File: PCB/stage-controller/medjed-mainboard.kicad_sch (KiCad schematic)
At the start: 28 parts, among them IC1 TMC429-LI, J1 Barrel_Jack, U1 RP2040

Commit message: Add initial version stage PCB
Will probably need major revisions as efforts towards TMC4361A will require significant changes.
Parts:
- removed U1: RP2040, Package_DFN_QFN:QFN-56-1EP_7x7mm_P0.4mm_EP3.2x3.2mm, symbol MCU_RaspberryPi:RP2040
- added C10, C11, C16, C7, C8, C9: 100nF, Capacitor_SMD:C_0603_1608Metric, symbol Device:C
- added C12, C17, C18, C19: 10uF, Capacitor_SMD:C_0805_2012Metric, symbol Device:C
- added C13: 22uF, Capacitor_SMD:C_0805_2012Metric, symbol Device:C
- added C14, C15, C20, C21: 1uF, Capacitor_SMD:C_0402_1005Metric, symbol Device:C
- added D1: SMAJ28CA, medjed-mainboard:SMAJ28CA, symbol Diode:5KPxxCA
- added D2, D3, D4, D5, D6, D7, D8: Red, LED_SMD:LED_0805_2012Metric, symbol Device:LED
- added F1: SMDC185F/33-2, medjed-mainboard:SMDC185F_33-2, symbol Device:Polyfuse
- added FB1: FerriteBead, medjed-mainboard:BLM41P600S, symbol Device:FerriteBead
- added J2: Conn_01x05, Connector_PinSocket_2.54mm:PinSocket_1x05_P2.54mm_Vertical, symbol Connector_Generic:Conn_01x05
- added JP1, JP5: SolderJumper_2_Open, Jumper:SolderJumper-2_P1.3mm_Open_RoundedPad1.0x1.5mm, symbol Jumper:SolderJumper_2_Open
- added JP2, JP3, JP4, JP6: SolderJumper_2_Bridged, Jumper:SolderJumper-2_P1.3mm_Bridged_RoundedPad1.0x1.5mm, symbol Jumper:SolderJumper_2_Bridged
- added R10, R11, R12, R14, R16, R17, R18: 5k1, Resistor_SMD:R_0603_1608Metric, symbol Device:R
- added R13, R15: 10k, Resistor_SMD:R_0603_1608Metric, symbol Device:R
- added SW1: SW_Push_SPDT, medjed-mainboard:switch_SS3NP-MS-V-TR, symbol Switch:SW_Push_SPDT
- added TP1, TP2, TP3, TP4, TP5, TP6: TestPoint_Small, TestPoint:TestPoint_Pad_D1.0mm, symbol Connector:TestPoint_Small
- added TP10, TP7, TP8, TP9: TestPoint, TestPoint:TestPoint_Pad_D1.0mm, symbol Connector:TestPoint
- added U1: P78E-1000, medjed-mainboard:P78E-1000, symbol medjed-mainboard:P78E05-1000
- added U11: teensy 4.1, medjed-mainboard:teensy_4.1, symbol medjed-mainboard:teensy 4.1
- added U12: MIC5317-3.3, Package_TO_SOT_SMD:SOT-23-5, symbol medjed-mainboard:MIC5317-3.3
- added U13: MIC5317-1.5, Package_TO_SOT_SMD:SOT-23-5, symbol medjed-mainboard:MIC5317-3.3
- J1: Voltage (none) -> 24V
- renumbered U7 to U5, U5 to U7
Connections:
- net +5V: now also C10.2, C11.2, C13.1, C14.1, C17.1, C18.1, C19.1, C20.1, C9.2, D3.2 (A), JP6.2 (B), TP7.1, U1.3 (Vout), U12.1 (Vin), U12.3 (EN), U13.1 (Vin), U13.3 (EN)
- net EN motors: now also SW1.2 (B)
- net GND: now also IC1.33 (DIE_PAD), ICe1.1 (GND@1), ICe1.12 (GND@3), ICe1.25 (GND@4), ICe1.38 (GND@5), ICe1.47 (TCK), ICe1.48 (TDI), ICe1.51 (GND@6), ICe1.67 (GND@7), ICe1.75 (GND@8), ICe1.88 (GND@9), ICe1.9 (GND@2), J1.2, U5.4 (GND), C10.1, C11.1, C12.2, C13.2, C14.2, C15.2, C16.2, C17.2, C18.2, C19.2, C20.2, C21.2, C7.2, C8.2, C9.1, D1.1 (A1), JP1.1 (A), JP5.1 (A), R10.2, R11.2, R12.2, R14.2, R16.2, R17.2, R18.2, U1.2 (GND), U11.GND1 (GND), U11.GND2 (GND), U11.GND3 (GND), U11.GND4 (GND), U11.GND5 (GND), U12.2 (GND), U13.2 (GND); no longer IC1.EXP (DIE_PAD)
- net X_Z-: now reaches R2.1, U8.1 (1B)
- net X_Z-: now also U5.11 (Z-); no longer U7.11 (Z-)
- net X_A+: now reaches R3.2, U8.10 (3A)
- net X_A+: now also U5.5 (A+); no longer U7.5 (A+)
- net ENC_A_X: now reaches U8.11 (3Y)
- net ENC_A_X: now also ICe1.10 (ENC3_A); no longer ICe1.3 (ENC1_A)
- net X_Z+: now reaches R2.2, U8.2 (1A)
- net X_Z+: now also U5.10 (Z+); no longer U7.10 (Z+)
- net ENC_N_X: now reaches U8.3 (1Y)
- net ENC_N_X: now also ICe1.13 (ENC3_N); no longer ICe1.5 (ENC1_N)
- net ENC_B_X: now reaches U8.5 (2Y)
- net ENC_B_X: now also ICe1.11 (ENC3_B); no longer ICe1.4 (ENC1_B)
- net X_B+: now reaches R1.2, U8.6 (2A)
- net X_B+: now also U5.7 (B+); no longer U7.7 (B+)
- net X_B-: now reaches R1.1, U8.7 (2B)
- net X_B-: now also U5.8 (B-); no longer U7.8 (B-)
- net X_A-: now reaches R3.1, U8.9 (3B)
- net X_A-: now also U5.6 (A-); no longer U7.6 (A-)
- net Z_Z+: now reaches R7.2, U10.2 (1A)
- net Z_Z+: now also U7.10 (Z+); no longer U5.10 (Z+)
- net Z_Z-: now reaches R7.1, U10.1 (1B)
- net Z_Z-: now also U7.11 (Z-); no longer U5.11 (Z-)
- net Z_A+: now reaches R9.2, U10.10 (3A)
- net Z_A+: now also U7.5 (A+); no longer U5.5 (A+)
- net Z_A-: now reaches R9.1, U10.9 (3B)
- net Z_A-: now also U7.6 (A-); no longer U5.6 (A-)
- net Z_B+: now reaches R8.2, U10.6 (2A)
- net Z_B+: now also U7.7 (B+); no longer U5.7 (B+)
- net Z_B-: now reaches R8.1, U10.7 (2B)
- net Z_B-: now also U7.8 (B-); no longer U5.8 (B-)
- net DIR-Z: now reaches IC1.17 (SCK_S_D1), U3.5 (DIR)
- net DIR-Z: now also TP5.1
- net STEP-Z: now reaches IC1.15 (SDO_S_S1), U3.6 (STEP)
- net STEP-Z: now also TP6.1
- net +24V: now reaches C5.2, C6.1, U3.7 (+24V)
- net +24V: now also C1.2, C2.1, C3.2, C4.1, U2.7 (+24V), U4.7 (+24V), C12.1, C8.1, D2.2 (A), FB1.2, TP8.1, U1.1 (Vin)
- net +24Vsrc: now reaches J1.1
- net +24Vsrc: now also F1.1
- net MOSI: now reaches IC1.10 (SDI_C), ICe1.99 (SDI)
- net MOSI: now also J2.4 (Pin_4), U11.26 (A12)
- net SDO-429: now reaches IC1.12 (SDOZ_C), ICe1.96 (SDO429)
- net SDO-429: now also JP2.1 (A)
- net INT_429: now reaches IC1.14 (~{INT_SDO_C})
- net INT_429: now also U11.10 (CS1)
- net STEP-Y: now reaches IC1.18 (~{SCS_S_S2}), U2.6 (STEP)
- net STEP-Y: now also TP3.1
- net STEP-X: now reaches IC1.19 (~{SCS2_S3}), U4.6 (STEP)
- net STEP-X: now also TP1.1
- net DIR-X: now reaches IC1.20 (~{SCS3_D3}), U4.5 (DIR)
- net DIR-X: now also TP2.1
- net +3.3V: now reaches IC1.21 (V5@2)
- net +3.3V: now also IC1.22 (V33), IC1.3 (V5@1), ICe1.18 (VCCI@1), ICe1.24 (VCC@1), ICe1.39 (VCCI@2), ICe1.50 (VCC@2), ICe1.52 (VCC@3), ICe1.56 (VCC@4), ICe1.66 (VCCI@3), ICe1.74 (VCC@5), ICe1.87 (VCCI@4), C15.1, C16.1, D4.2 (A), JP3.2 (B), JP4.1 (A), R13.1, TP9.1, U12.5 (Vout)
- net DIR-Y: now reaches IC1.27 (SDI_S_D2), U2.5 (DIR)
- net DIR-Y: now also TP4.1
- net POSCMP: now reaches IC1.30 (POSCMP)
- net POSCMP: now also D5.2 (A)
- net TeensyCLK: now reaches IC1.5 (CLK)
- net TeensyCLK: now also ICe1.64 (CLK), U11.40 (A16)
- net CS429: now reaches IC1.7 (~{SCS_C}), ICe1.95 (~{SCS429})
- net CS429: now also J2.1 (Pin_1), U11.25 (A11)
- net SCK: now reaches IC1.8 (SCK_C), ICe1.98 (SCK)
- net SCK: now also J2.3 (Pin_3), U11.27 (A13)
- net ENC_A_Z: now reaches U10.11 (3Y)
- net ENC_A_Z: now also ICe1.3 (ENC1_A); no longer ICe1.10 (ENC3_A)
- net MISO: now reaches ICe1.100 (SDO)
- net MISO: now also J2.5 (Pin_5), JP2.2 (B), U11.39 (A15)
- net ENC_B_Z: now reaches U10.5 (2Y)
- net ENC_B_Z: now also ICe1.4 (ENC1_B); no longer ICe1.11 (ENC3_B)
- net ENC_N_Z: now reaches U10.3 (1Y)
- net ENC_N_Z: now also ICe1.5 (ENC1_N); no longer ICe1.13 (ENC3_N)
- net +1V5: now reaches ICe1.14 (VCORE@1)
- net +1V5: now also ICe1.17 (VCORE@2), ICe1.37 (VCORE@3), ICe1.68 (VCORE@4), ICe1.89 (VCORE@5), C21.1, TP10.1, U13.5 (Vout)
- net at ICe1.49 (TMS): now also ICe1.55 (TRST), R13.2
- net ENC_A_Y: now reaches ICe1.6 (ENC2_A), U9.11 (3Y)
- net ENC_B_Y: now reaches ICe1.7 (ENC2_B), U9.5 (2Y)
- net ENC_N_Y: now reaches ICe1.8 (ENC2_N), U9.3 (1Y)
- net at ICe1.86 (ENC_INV): now also JP1.2 (B)
- net at ICe1.92 (EXT_RES): now also JP3.1 (A)
- net INT_424: now reaches ICe1.94 (~{INT})
- net INT_424: now also U11.16 (A2)
- net CS424: now reaches ICe1.97 (~{SCS})
- net CS424: now also J2.2 (Pin_2), U11.38 (A14)
- net Y_Z-: now reaches R4.1, U6.11 (Z-), U9.1 (1B)
- net Y_Z+: now reaches R4.2, U6.10 (Z+), U9.2 (1A)
- net Y_A+: now reaches R6.2, U6.5 (A+), U9.10 (3A)
- net Y_B+: now reaches R5.2, U6.7 (B+), U9.6 (2A)
- net Y_B-: now reaches R5.1, U6.8 (B-), U9.7 (2B)
- net Y_A-: now reaches R6.1, U6.6 (A-), U9.9 (3B)
- new net: D3.1 (K), R10.1
- new net: R15.1, SW1.1 (A)
- new net: D7.1 (K), R17.1
- new net: D4.1 (K), R12.1
- new net: D2.1 (K), R11.1
- new net: D8.1 (K), R18.1
- new net: D5.1 (K), R14.1
- new net: U11.3.3V_1 (3.3V), U11.3.3V_2 (3.3V), U11.3.3V_3 (3.3V)
- new net: U11.USB_GND1 (USB_GND), U11.USB_GND2 (USB_GND)
- new net: JP6.1 (A), U11.VIN
- new net: D6.1 (K), R16.1
- new net +24Vfused: C7.1, D1.2 (A2), F1.2, FB1.1
- new net HomeX: D6.2 (A), U11.36 (CS2)
- new net HomeY: D7.2 (A), U11.35 (TX8)
- new net HomeZ: D8.2 (A), U11.34 (RX8)
- new net STEPPER_EN: SW1.3 (C), U11.33 (MCLK2)
- new net STEP_EN_MANUAL: JP4.2 (B), JP5.2 (B), R15.2
- no-connect marks 6 -> 30
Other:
- note added: "0.0.1"
- note added: "27-04-2023"
- note added: "Figure out GBAR stuff"
- note added: "Medjed Stage Controller Board"
- note added: "PWM clock signal 18.75MHz?"
- note added: "Remember to cut solder jumper on Teensy if powering from 5V"
- note added: "Run in 3.3V supply mode (CMOS)"
- note added: "TMC2209 is off with ENN input high Unknown if Snapmaker EN is inverted"
- note added: "TODO: remove bridged jumper"
- note added: "To be used with Teensy 4.1 board"
- note added: "should not be needed"
- note removed: "handle these two"
- moved on the sheet: C1, C2, C3, C4, C5, C6, ICe1, J1, R1, R2, R3, R4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

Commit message: New TMC4361 design
Redesigned stage controller around the TMC4361.
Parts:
- removed C1, C17, C18, C19, C3, C5: 10uF, Capacitor_SMD:C_0805_2012Metric, symbol Device:C
- removed C11, C16, C9: 100nF, Capacitor_SMD:C_0603_1608Metric, symbol Device:C
- removed C2, C4, C6: 220uF, medjed-mainboard:CP_Elec_220uf, symbol Device:C_Polarized
- removed D5, D6, D7, D8: Red, LED_SMD:LED_0805_2012Metric, symbol Device:LED
- removed IC1: TMC429-LI, Package_DFN_QFN:QFN-32-1EP_5x5mm_P0.5mm_EP3.3x3.3mm, symbol medjed-mainboard:TMC429-LI
- removed ICe1: TMC424, TQFP100, symbol medjed-mainboard:TMC424
- removed J2: Conn_01x05, Connector_PinSocket_2.54mm:PinSocket_1x05_P2.54mm_Vertical, symbol Connector_Generic:Conn_01x05
- removed JP1, JP5: SolderJumper_2_Open, Jumper:SolderJumper-2_P1.3mm_Open_RoundedPad1.0x1.5mm, symbol Jumper:SolderJumper_2_Open
- removed R1, R2, R3, R4, R5, R6, R7, R8: 120, Resistor_SMD:R_0402_1005Metric_Pad0.72x0.64mm_HandSolder, symbol Device:R_Small
- removed R13, R15: 10k, Resistor_SMD:R_0603_1608Metric, symbol Device:R
- removed R14, R16, R17, R18: 5k1, Resistor_SMD:R_0603_1608Metric, symbol Device:R
- removed SW1: SW_Push_SPDT, medjed-mainboard:switch_SS3NP-MS-V-TR, symbol Switch:SW_Push_SPDT
- removed TP1, TP2, TP3, TP4, TP5, TP6: TestPoint_Small, TestPoint:TestPoint_Pad_D1.0mm, symbol Connector:TestPoint_Small
- removed U10, U8, U9: ~, medjed-mainboard:TSSOP-16-AM26LS32A, symbol medjed-mainboard:AM26LS32ACPWR
- removed U2, U3, U4: ~, medjed-mainboard:snapmaker_8-pin, symbol medjed-mainboard:Snapmaker_8-pin
- removed U5, U6, U7: ~, medjed-mainboard:Molex 52745-1197, symbol medjed-mainboard:Molex_52745-1197
- added C26: 4.7nF, Capacitor_SMD:C_0603_1608Metric, symbol Device:C_Small
- added J2: ESTOP terminal, TerminalBlock_TE-Connectivity:TerminalBlock_TE_282834-2_1x02_P2.54mm_Horizontal, symbol Connector:Screw_Terminal_01x02
- added J3: Conn_01x04_Pin, Connector_JST:JST_SH_BM04B-SRSS-TB_1x04-1MP_P1.00mm_Vertical, symbol Connector:Conn_01x04_Pin
- added JP1, JP5, JP7: SolderJumper_2_Bridged, Jumper:SolderJumper-2_P1.3mm_Bridged_RoundedPad1.0x1.5mm, symbol Jumper:SolderJumper_2_Bridged
- added R13: 120, Resistor_SMD:R_0603_1608Metric, symbol Device:R_Small
- added R14: 60, Resistor_SMD:R_0603_1608Metric, symbol Device:R_Small
- added SW2: ESTOP switch, medjed-mainboard:E-switch-button, symbol Switch:SW_MEC_5E
- added U10: TCAN330, Package_SO:SOIC-8_3.9x4.9mm_P1.27mm, symbol Interface_CAN_LIN:TCAN330
- D1: footprint medjed-mainboard:SMAJ28CA -> Diode_THT:D_P600_R-6_P20.00mm_Horizontal
- R9: value 120 -> 60; footprint Resistor_SMD:R_0402_1005Metric_Pad0.72x0.64mm_HandSolder -> Resistor_SMD:R_0603_1608Metric; Mouser 667-ERA-2AED121X -> (none); now fitted
- U11: footprint medjed-mainboard:teensy_4.1 -> MODULE_DEV-16771; MANUFACTURER (none) -> SparkFun Electronics; MAXIMUM_PACKAGE_HEIGHT (none) -> 4.07mm; PARTREV (none) -> 4.1; STANDARD (none) -> Manufacturer recommendations
- U13: value MIC5317-1.5 -> MIC5317-1.8; Mouser 998-MIC5317-1.5YM5TR -> 998-MIC5317-1.8YM5TR
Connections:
- net Z_A- is gone; now on net CAN_H: R9.1
- net +3.3V: now also C10.1, J3.3 (Pin_3), U10.3 (VCC); no longer JP3.2 (B), JP4.1 (A)
- net +5V: no longer C10.2
- net GND: now also C10.2, C26.1, J2.1 (Pin_1), J3.4 (Pin_4), SW2.1, U10.2 (GND); no longer C10.1
- net MISO: no longer JP2.2 (B)
- net TeensyCLK: now also U11.32 (OUT1B); no longer U11.40 (A16)
- net Axis Y/CAN_L: now reaches JP3.1 (A)
- net at U11.0 (RX1): now also U10.4 (RXD)
- net at U11.1 (TX1): now also U10.1 (TXD)
- net EN_SNAP: now reaches U11.12 (MISO)
- net CAN_EN: now reaches U11.2 (OUT2)
- net CAN_EN: now also U10.5 (SHDN)
- net SCL: now reaches U11.24 (A10)
- net SCL: now also J3.1 (Pin_1)
- net INT_X: now reaches U11.28 (RX7)
- net INT_Y: now reaches U11.29 (TX7)
- net INT_Z: now reaches U11.30 (CRX3)
- net CS_Y: now reaches U11.37 (CS3)
- net +1V5 renamed +1V8
- net CS424 renamed CS_Z
- net CS429 renamed SDA
- net SDA: now also J3.2 (Pin_2)
- net HomeX renamed CS_X
- net HomeY renamed RST_AXES
- net HomeZ renamed SAFETY
- net SAFETY: now also J2.2 (Pin_2), SW2.3 (K), SW2.4 (A)
- net INT_424: no longer names the net of U11.16 (A2)
- net INT_429: no longer names the net of U11.10 (CS1)
- net SDO-429 renamed Axis Z/CAN_L
- net STEPPER_EN: no longer names the net of U11.33 (MCLK2)
- net STEP_EN_MANUAL renamed CAN_H
- net CAN_H: now also JP1.2 (B), JP5.2 (B), R13.1, U10.7 (CANH)
- net Z_A+: no longer names the net of R9.2
- net Z_A+: now also C26.2, R14.1
- new net Axis X/CAN_H: JP5.1 (A)
- new net Axis X/CAN_L: JP7.1 (A)
- new net Axis Y/CAN_H: JP4.1 (A)
- new net Axis Z/CAN_H: JP1.1 (A)
- new net CAN_L: JP2.2 (B), JP3.2 (B), JP7.2 (B), R13.2, R14.2, U10.6 (CANL)
- no-connect marks 30 -> 2
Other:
- added sheet Axis X (enc_axis.kicad_sch)
- added sheet Axis Y (enc_axis.kicad_sch)
- added sheet Axis Z (enc_axis.kicad_sch)
- note added: "0.1.2"
- note added: "SnapMaker cables are terminated at end"
- note added: "Snapmaker Linear Axes Cable is 40cm; a little long for CAN stub but probably acceptable"
- note removed: "0.0.1"
- note removed: "Figure out GBAR stuff"
- note removed: "Run in 3.3V supply mode (CMOS)"
- note removed: "TMC2209 is off with ENN input high Unknown if Snapmaker EN is inverted"
- note removed: "TODO: remove bridged jumper"
- note removed: "X-axis"
- note removed: "Y-axis"
- note removed: "Z-axis"
- note removed: "should not be needed"
- moved on the sheet: C20, C21, JP6, TP10, U11, U13

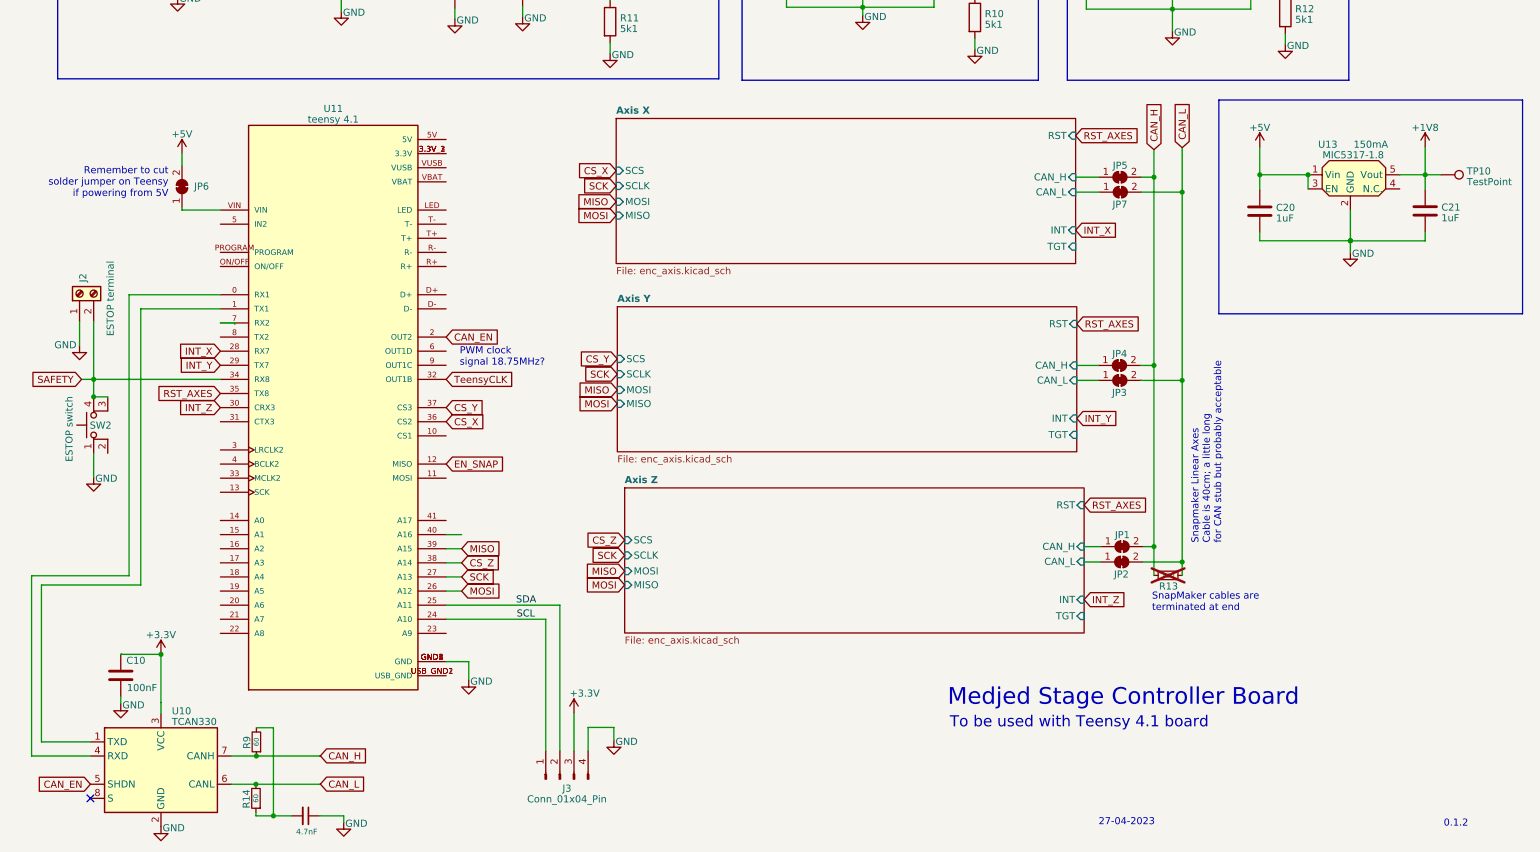
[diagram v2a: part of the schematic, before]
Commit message: Finalise part numbers and I2C pullup
Complete mouser part numbers. Added pullup for I2C connector.
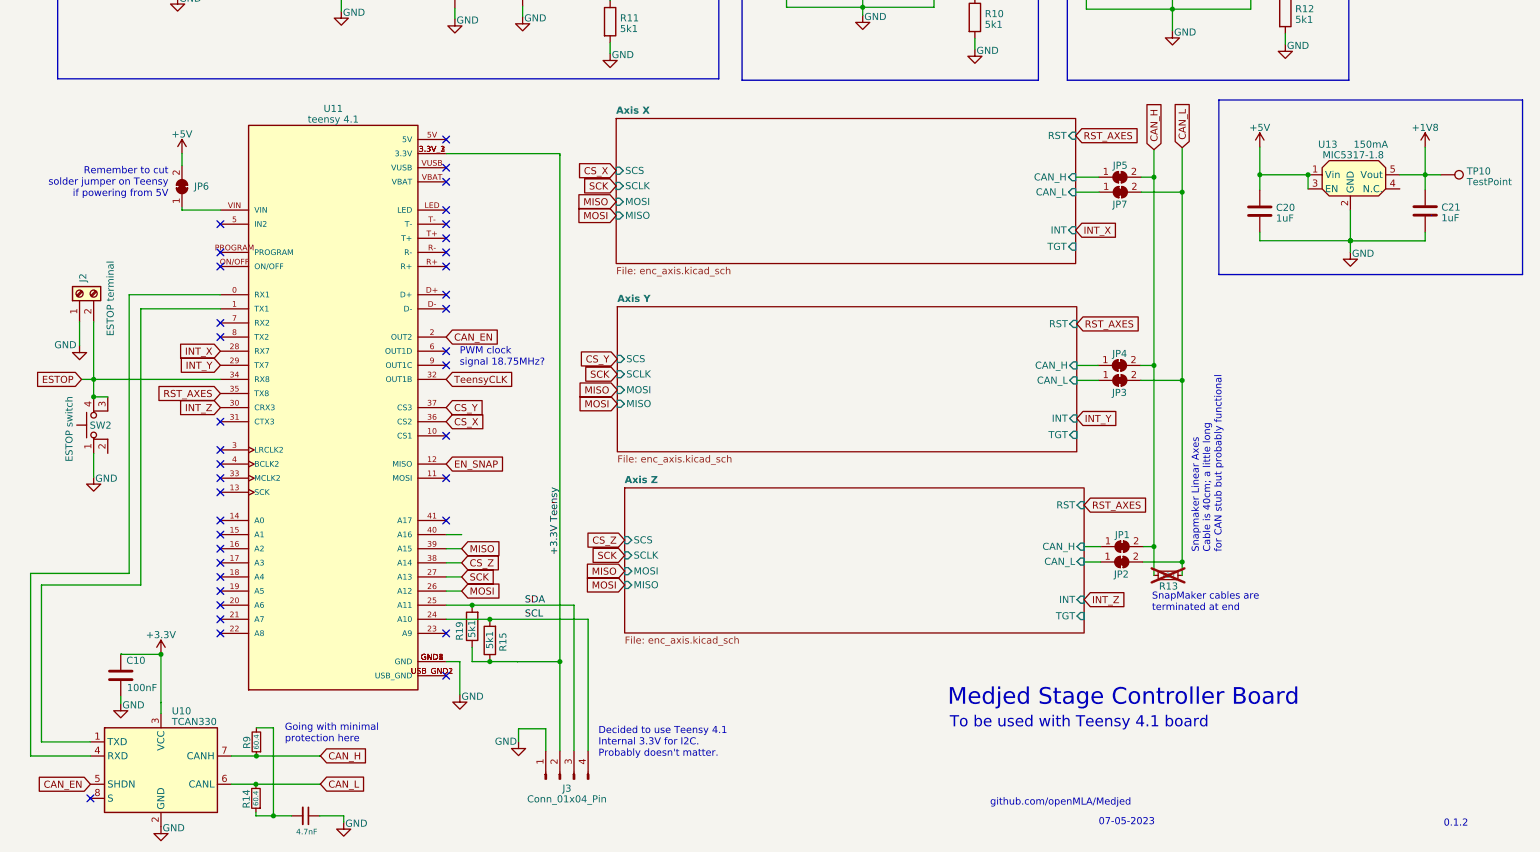
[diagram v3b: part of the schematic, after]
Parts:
- added R15, R19: 5k1, Resistor_SMD:R_0603_1608Metric, symbol Device:R
- C10, C7, C8: Mouser (none) -> 810-C1608X7R1H104KEP
- C26: Mouser 80-C603C104K5RAC3121 -> 810-C1608NP01H4R7C0A
- J2: Mouser (none) -> 649-VN02A15000J0G
- J3: Mouser (none) -> 485-4328
- R13: Mouser (none) -> 667-ERA-3AED121V
- R14, R9: value 60 -> 60.4; Mouser (none) -> 667-ERA-3AEB60R4V
- U10: Mouser (none) -> 595-TCAN330D
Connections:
- net +3.3V: no longer J3.3 (Pin_3)
- net GND: now also J3.1 (Pin_1); no longer J3.4 (Pin_4)
- net SCL: now also J3.4 (Pin_4), R15.2; no longer J3.1 (Pin_1)
- net SDA: now also J3.3 (Pin_3), R19.2; no longer J3.2 (Pin_2)
- net +3.3V Teensy: now reaches U11.3.3V_1 (3.3V), U11.3.3V_2 (3.3V), U11.3.3V_3 (3.3V)
- net +3.3V Teensy: now also J3.2 (Pin_2), R15.1, R19.1
- net SAFETY renamed ESTOP
- no-connect marks 2 -> 38
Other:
- note added: "07-05-2023"
- note added: "Decided to use Teensy 4.1 Internal 3.3V for I2C. Probably doesn't matter."
- note added: "Going with minimal protection here"
- note added: "Snapmaker Linear Axes Cable is 40cm; a little long for CAN stub but probably functional"
- note added: "github.com/openMLA/Medjed"
- note removed: "27-04-2023"
- note removed: "Snapmaker Linear Axes Cable is 40cm; a little long for CAN stub but probably acceptable"

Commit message: Update PCB files
Pre-removal and submodule reorganisation
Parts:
- C12: Mouser 810-C2012X7S1E106125 -> 810-C2012X5R1H106K12
- C26: Mouser 810-C1608NP01H4R7C0A -> 810-C1608C0G1H472J08
- D1: footprint Diode_THT:D_P600_R-6_P20.00mm_Horizontal -> medjed-mainboard:SMAJ28CA
- J1: Mouser (none) -> 490-PJ-002B
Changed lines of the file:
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@@
       (effects (font (size 1.27 1.27)) hide)
     )
-    (property "Datasheet" "~" (at 31.877 39.878 0)
+    (property "Datasheet" "https://nl.mouser.com/datasheet/2/670/pj_002b-1778766.pdf" (at 31.877 39.878 0)
       (effects (font (size 1.27 1.27)) hide)
     )
     (property "Voltage" "24V" (at 39.751 35.306 0)
+      (effects (font (size 1.27 1.27)) hide)
+    )
+    (property "Mouser" "490-PJ-002B" (at 30.607 38.862 0)
       (effects (font (size 1.27 1.27)) hide)
     )
@@
       (effects (font (size 1.27 1.27)) hide)
     )
-    (property "Datasheet" "https://product.tdk.com/system/files/dam/doc/product/capacitor/ceramic/mlcc/catalog/mlcc_automotive_epoxy_en.pdf?ref_disty=mouser" (at 102.87 42.545 0)
+    (property "Datasheet" "https://product.tdk.com/system/files/dam/doc/product/capacitor/ceramic/mlcc/catalog/mlcc_automotive_epoxy_en.pdf" (at 102.87 42.545 0)
       (effects (font (size 1.27 1.27)) hide)
     )
@@
       (effects (font (size 1.27 1.27)) hide)
     )
-    (property "Mouser" "810-C2012X7S1E106125" (at 150.368 40.894 0)
+    (property "Mouser" "810-C2012X5R1H106K12" (at 150.368 40.894 0)
       (effects (font (size 1.27 1.27)) hide)
     )
@@
       (effects (font (size 1.27 1.27)) hide)
     )
-    (property "Datasheet" "https://product.tdk.com/system/files/dam/doc/product/capacitor/ceramic/mlcc/catalog/mlcc_automotive_epoxy_en.pdf?ref_disty=mouser" (at 30.5308 166.8161 0)
+    (property "Datasheet" "https://product.tdk.com/system/files/dam/doc/product/capacitor/ceramic/mlcc/catalog/mlcc_automotive_epoxy_en.pdf" (at 30.5308 166.8161 0)
       (effects (font (size 1.27 1.27)) hide)
     )
@@
       (effects (font (size 1.27 1.27)) hide)
     )
-    (property "Datasheet" "https://product.tdk.com/system/files/dam/doc/product/capacitor/ceramic/mlcc/catalog/mlcc_automotive_epoxy_en.pdf?ref_disty=mouser" (at 90.678 42.926 0)
+    (property "Datasheet" "https://product.tdk.com/system/files/dam/doc/product/capacitor/ceramic/mlcc/catalog/mlcc_automotive_epoxy_en.pdf" (at 90.678 42.926 0)
       (effects (font (size 1.27 1.27)) hide)
     )
@@
       (effects (font (size 1.27 1.27)) hide)
     )
-    (property "Datasheet" "https://product.tdk.com/system/files/dam/doc/product/capacitor/ceramic/mlcc/catalog/mlcc_commercial_hightemp_en.pdf" (at 63.8048 192.1002 0)
-      (effects (font (size 1.27 1.27)) hide)
-    )
-    (property "Mouser" "810-C1608NP01H4R7C0A" (at 63.8048 192.1002 0)
+    (property "Datasheet" "~" (at 63.8048 192.1002 0)
+      (effects (font (size 1.27 1.27)) hide)
+    )
+    (property "Mouser" "810-C1608C0G1H472J08" (at 63.8048 192.1002 0)
       (effects (font (size 1.27 1.27)) hide)
     )
@@
       (effects (font (size 1.27 1.27)) (justify right))
     )
-    (property "Footprint" "Diode_THT:D_P600_R-6_P20.00mm_Horizontal" (at 75.311 40.132 0)
-      (effects (font (size 1.27 1.27)) hide)
-    )
-    (property "Datasheet" "https://diotec.com/tl_files/diotec/files/pdf/datasheets/5kp65.pdf" (at 70.231 40.132 0)
+    (property "Footprint" "medjed-mainboard:SMAJ28CA" (at 75.311 40.132 0)
+      (effects (font (size 1.27 1.27)) hide)
+    )
+    (property "Datasheet" "https://nl.mouser.com/datasheet/2/240/Littelfuse_TVS_Diode_SMAJ_Datasheet_pdf-540740.pdf" (at 70.231 40.132 0)
       (effects (font (size 1.27 1.27)) hide)
     )
@@
       (effects (font (size 1.27 1.27)) hide)
     )
-    (property "Datasheet" "~" (at 109.5756 185.4962 0)
-      (effects (font (size 1.27 1.27)) hide)
-    )
+    (property "Datasheet" "https://nl.mouser.com/datasheet/2/737/4328_C13916_001_CCSH_W10_04_BK_RC_A-2490211.pdf" (at 109.5756 185.4962 0)
+      (effects (font (size 1.27 1.27)) hide)
+    )
